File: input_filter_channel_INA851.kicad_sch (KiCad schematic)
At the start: 15 parts, among them K1 EC2-12TNU, U104 INA851

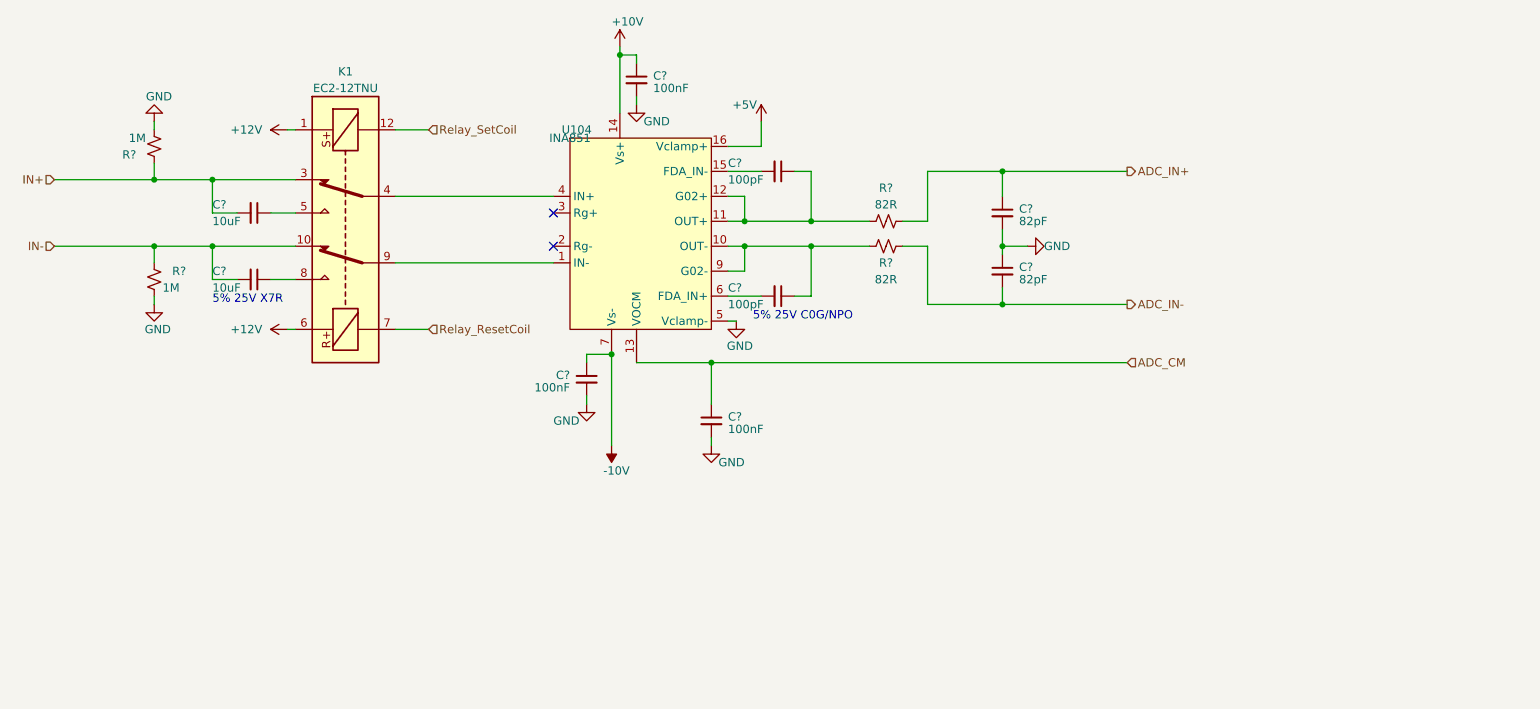
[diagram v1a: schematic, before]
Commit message: Updated Schematics
Changes:
-Moved Input resistors to after Coupling Relay
-Added diff cap at ADC input
-Changed the ADC clocking configuration (added quad LVDS driver)
-Changed some signal names for consistancy
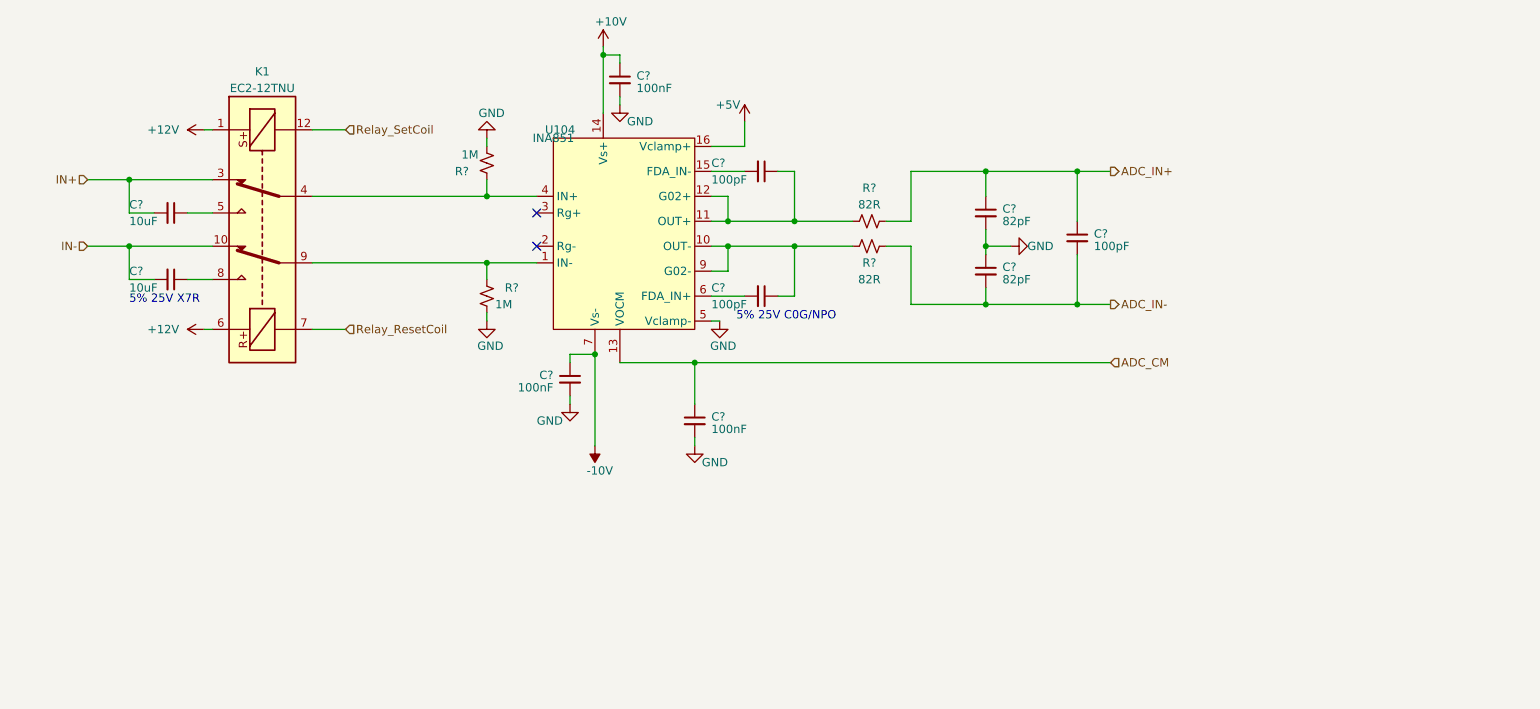
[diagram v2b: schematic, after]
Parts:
- added C?: 100pF, Capacitor_SMD:C_0603_1608Metric, symbol Device:C_Small
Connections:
- net ADC_IN+: now also C?.1
- net ADC_IN-: now also C?.2
- net IN+: no longer R?.2
- net IN-: no longer R?.2
- net at K1.9, U104.1 (IN-): now also R?.2
- net at K1.4, U104.4 (IN+): now also R?.2
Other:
- moved on the sheet: C?, K1, R?, U104

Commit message: Updated Schematics with latest suggestions
updates:
-Revised Power supply section
-Changed clock buffer chip for ADC Clock
- Added additional no pop & jumper parts for board debugging
-Other small part changes
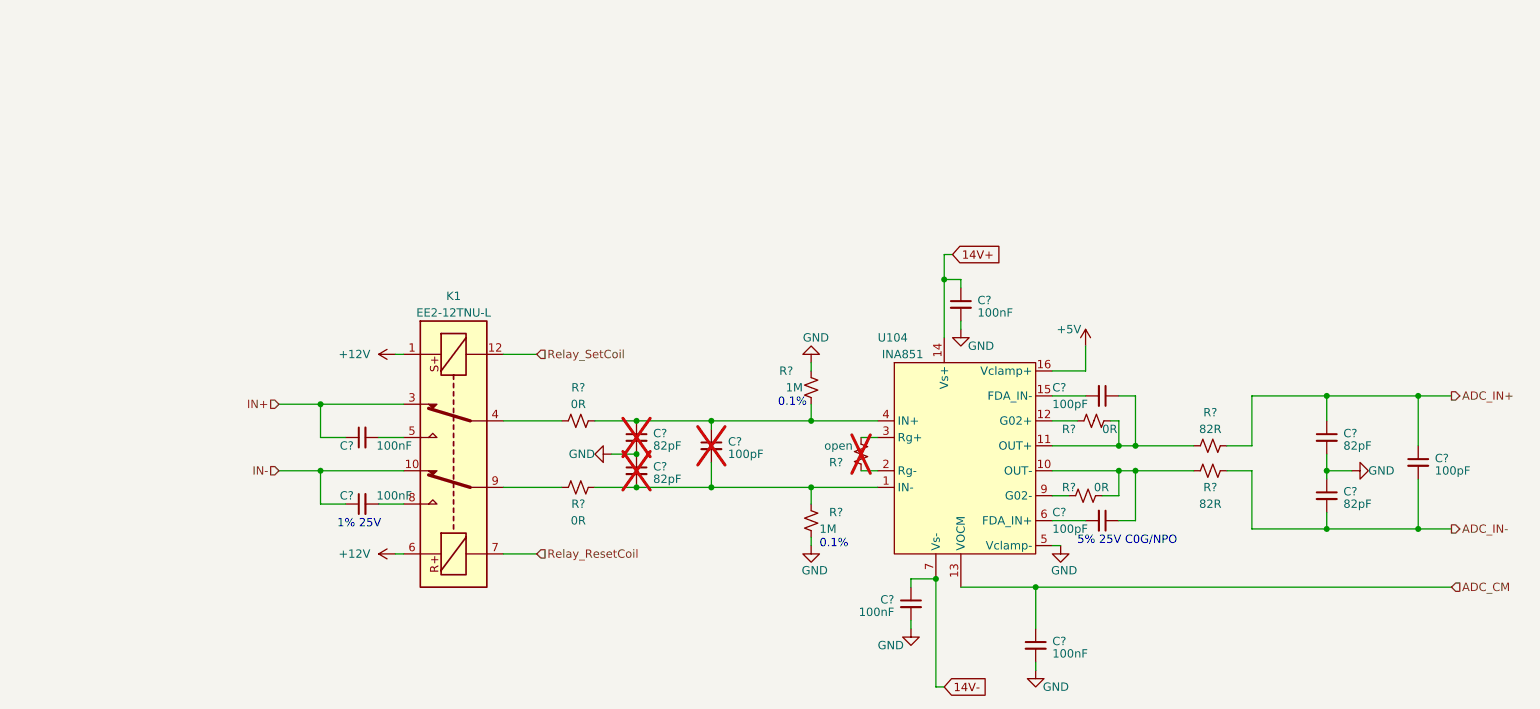
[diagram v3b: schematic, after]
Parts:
- removed C? (x2): 10uF, symbol Device:C_Small
- added C? (x2): 100nF, Capacitor_SMD:C_0603_1608Metric, symbol Device:C_Small
- added C?: 100pF, Capacitor_SMD:C_0603_1608Metric, symbol Device:C_Small
- added C? (x2): 82pF, Capacitor_SMD:C_0603_1608Metric, symbol Device:C_Small
- added R?: open, Resistor_SMD:R_0603_1608Metric, symbol Device:R_Small_US
- added R? (x2): 0R, Resistor_SMD:R_0603_1608Metric, symbol Device:R_Small_US
- added R? (x2): 0R, Capacitor_SMD:C_0603_1608Metric, symbol Device:R_Small_US
- K1: value EC2-12TNU -> EE2-12TNU-L; MPN (none) -> EE2-12TNU-L
- R? (x2): MPN RR0816P-105-D -> CPF0603B1M0E1
- U104: MPN (none) -> INA851RGTR
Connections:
- net GND: now also C?.1, C?.2
- net IN+: now also C?.1
- net IN-: now also C?.1
- net at R?.2, U104.4 (IN+): now also C?.1, C?.1, R?.2; no longer K1.4
- net at K1.8: now also C?.2
- net at C?.1, R?.1, U104.10 (OUT-): now also R?.2; no longer U104.9 (G02-)
- net at R?.2, U104.1 (IN-): now also C?.2, C?.2, R?.2; no longer K1.9
- net at C?.1, R?.1, U104.11 (OUT+): now also R?.2; no longer U104.12 (G02+)
- net at U104.2 (Rg-): now also R?.2
- net at U104.3 (Rg+): now also R?.1
- net at K1.5: now also C?.2
- net +10V renamed 14V+
- net -10V renamed 14V-
- new net: R?.1, U104.9 (G02-)
- new net: R?.1, U104.12 (G02+)
- new net: K1.4, R?.1
- new net: K1.9, R?.1
- no-connect marks 2 -> 0
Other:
- note added: "0.1%"
- note added: "1% 25V"
- note removed: "5% 25V X7R"
- moved on the sheet: C?, K1, R?, U104

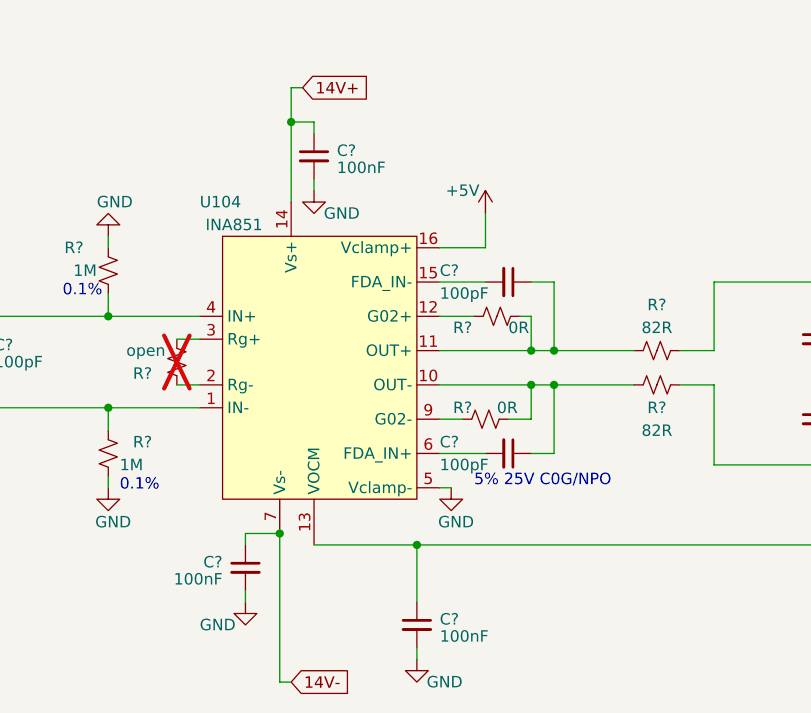
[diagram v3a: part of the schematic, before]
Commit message: Schematic Updates
Updated:
-Fixed AMC7823 labels
-Added present detect signals on FMC
-Added ferrite beads in Power Section and AFE
-Added 0R in power section
-Revised EEPROM connections
-Changed +5V SMPS part to one with an integrated inductor
-Added more detail on FMC connector
-Added file showing SMPS calculations
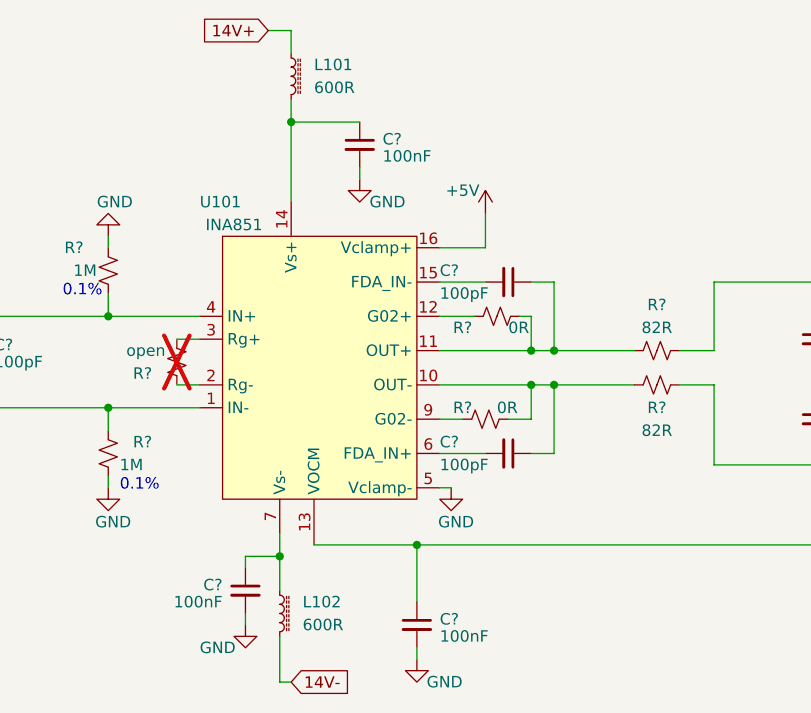
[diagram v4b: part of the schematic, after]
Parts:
- added L101, L102: 600R, symbol Device:L_Ferrite_Small
- renumbered U104 to U101
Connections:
- net 14V+: now also L101.1; no longer C?.1, U101.14 (Vs+)
- net 14V-: now also L102.2; no longer C?.1, U101.7 (Vs-)
- new net: C?.1, L101.2, U101.14 (Vs+)
- new net: C?.1, L102.1, U101.7 (Vs-)
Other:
- note removed: "5% 25V C0G/NPO"
- moved on the sheet: C?

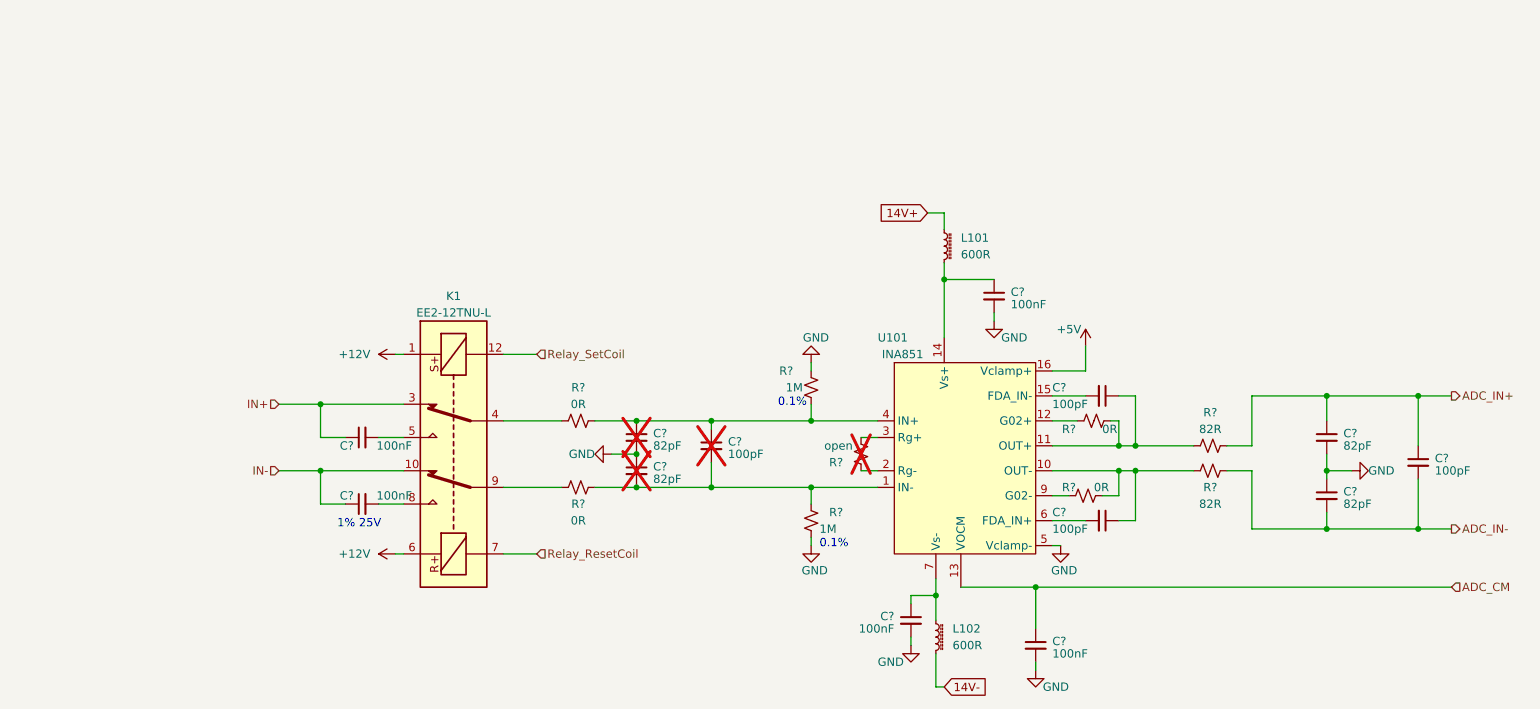
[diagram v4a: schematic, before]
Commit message: Updated Schematic
-Changed PPS input signal buffer
-Made Tweaks to Power Supply section  (Many involving the LT3097) as suggested by Trent.
- general schematic clean up for readability
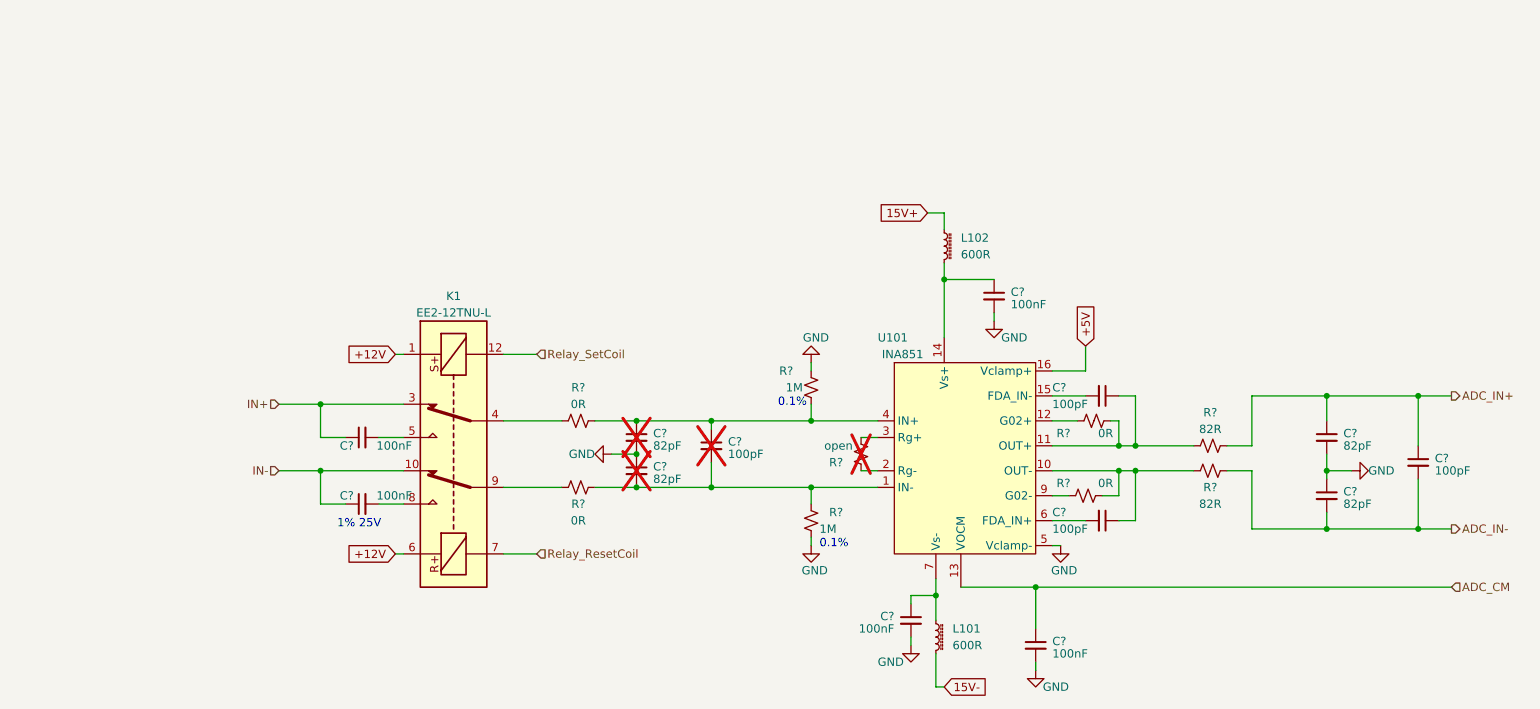
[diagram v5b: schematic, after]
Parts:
- removed R? (x2): 0R, Resistor_SMD:R_0603_1608Metric, symbol Device:R_Small_US
- added R? (x2): 0R, Resistor_SMD:R_0603_1608Metric, symbol Device:R_Small_US
- C?: MPN 0603N820J500CT -> GCM1885C1H101JA16D
- C? (x2): MPN C1206C106J3RACAUTO -> GRM1885C1H101JA01D
- R? (x2): footprint Capacitor_SMD:C_0603_1608Metric -> Resistor_SMD:R_0603_1608Metric; MPN (none) -> ERJ-3GEY0R00V
- R? (x2): footprint Capacitor_SMD:C_0603_1608Metric -> Resistor_SMD:R_0603_1608Metric; MPN (none) -> RC0603FR-0782RL
- renumbered L102 to L101, L101 to L102
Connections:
- net at C?.1, R?.1, U101.10 (OUT-): now also R?.2
- net at U101.9 (G02-): now also R?.1
- net at C?.1, R?.1, U101.11 (OUT+): now also R?.2
- net at U101.12 (G02+): now also R?.1
- net 14V+ renamed 15V+
- net 14V- renamed 15V-

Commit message: Update to Schematics; initial PCB commit
-Updated Power, Housekeeping, and ADCs sheets.
-Remapped FMC pins
-Initial board layout commit
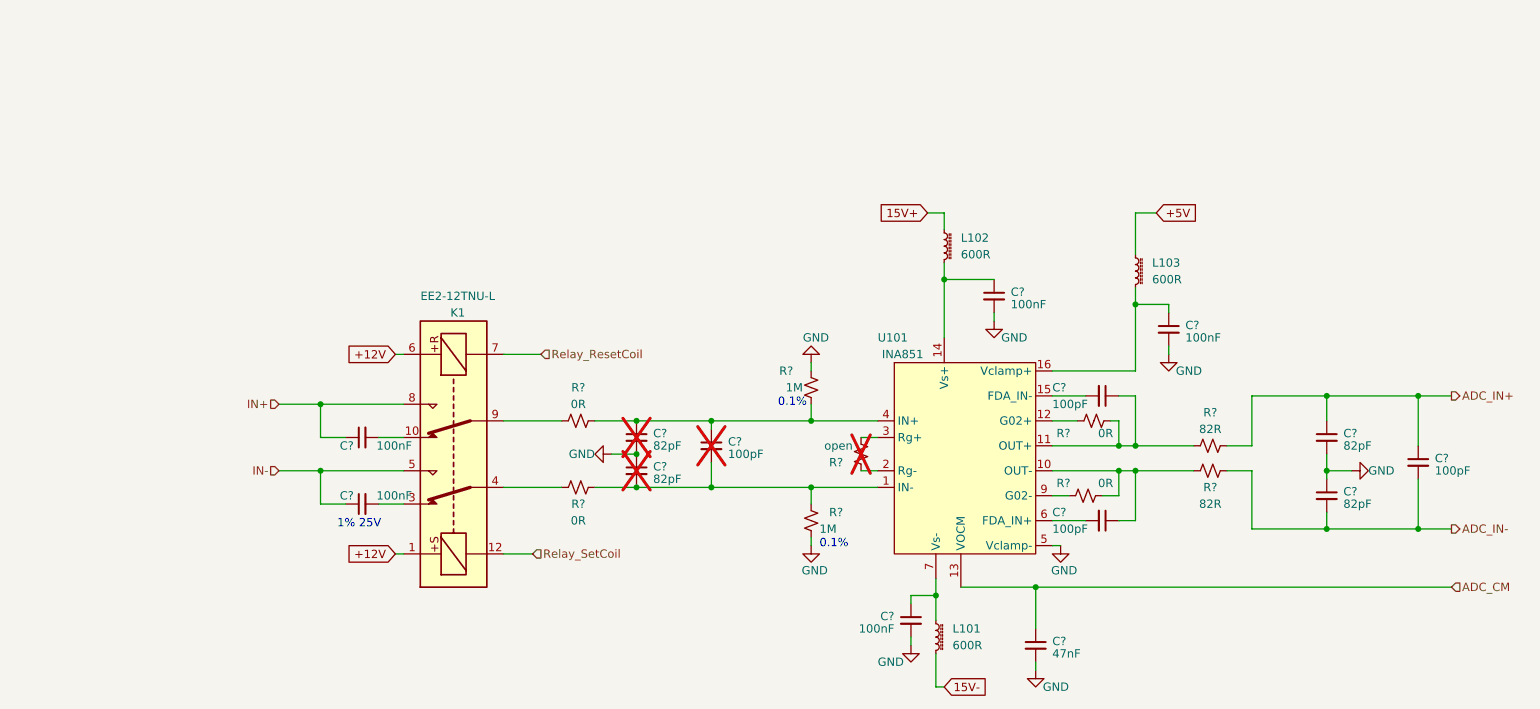
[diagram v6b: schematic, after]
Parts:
- added C?: 100nF, Capacitor_SMD:C_0402_1005Metric, symbol Device:C_Small
- added L103: 600R, Inductor_SMD:L_0402_1005Metric, symbol Device:L_Ferrite_Small
- C? (x8): footprint Capacitor_SMD:C_0603_1608Metric -> Capacitor_SMD:C_0402_1005Metric
- C? (x2): footprint (none) -> Capacitor_SMD:C_0402_1005Metric
- C?: value 100nF -> 47nF; footprint Capacitor_SMD:C_0603_1608Metric -> Capacitor_SMD:C_0402_1005Metric; MPN CL10B104KB8NNWC -> (none)
- L101, L102: footprint (none) -> Inductor_SMD:L_0402_1005Metric; MPN BLM18AG601SN1D -> BLM15AX601SN1D
- R? (x7): footprint Resistor_SMD:R_0603_1608Metric -> Resistor_SMD:R_0402_1005Metric
- U101: footprint (none) -> Package_DFN_QFN:QFN-16-1EP_3x3mm_P0.5mm_EP1.75x1.75mm_ThermalVias
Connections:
- net +5V: now also L103.1; no longer U101.16 (Vclamp+)
- net GND: now also C?.2
- net IN+: now also K1.8; no longer K1.3
- net IN-: now also K1.5; no longer K1.10
- net at C?.2: now also K1.3; no longer K1.8
- net at R?.1: now also K1.9; no longer K1.4
- net at R?.1: now also K1.4; no longer K1.9
- net at C?.2: now also K1.10; no longer K1.5
- new net: C?.1, L103.2, U101.16 (Vclamp+)
